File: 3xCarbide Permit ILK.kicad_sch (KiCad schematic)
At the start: 54 parts, among them J1 UT00104PH, J2 UT00104PH, J3 UT00104PH, J4 UT00104PH, J5 UT00104PH, J6 UT00104PH, SW1 2PB11, SW2 2PB11, SW3 2PB11, SW4 2PB11, SW5 2PB11, SW6 2PB11

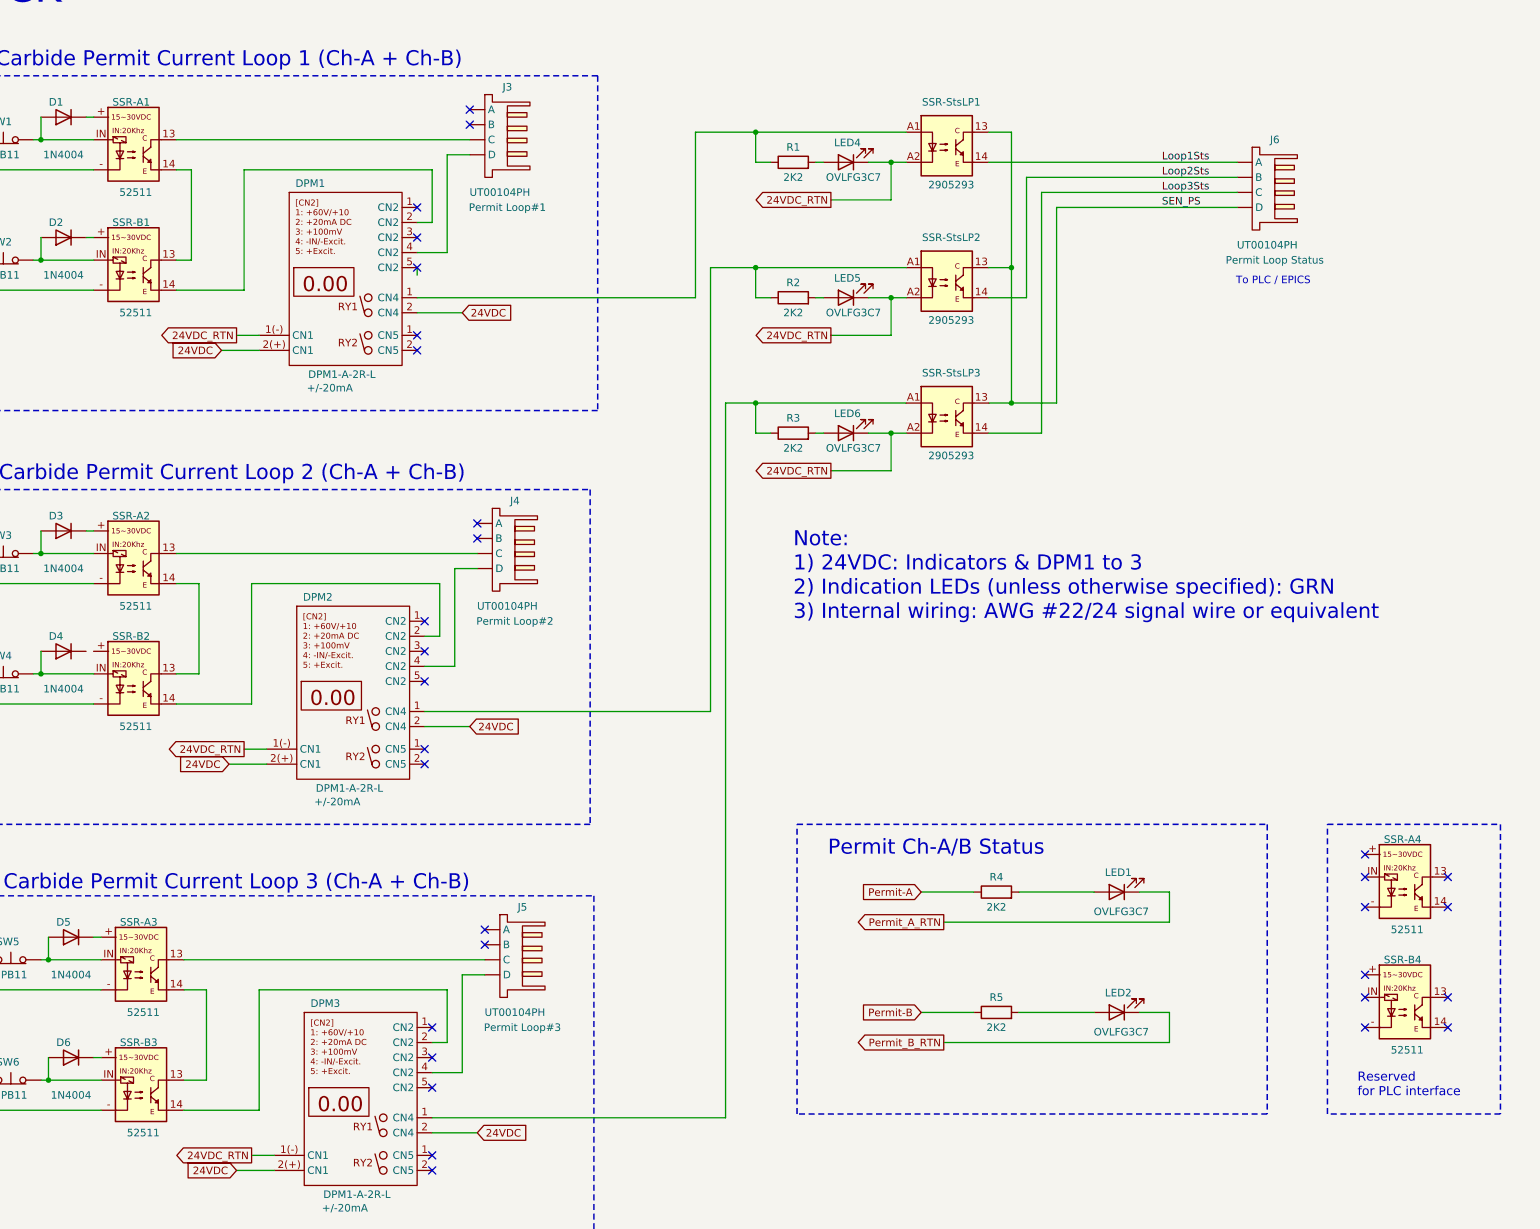
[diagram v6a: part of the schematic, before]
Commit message: updated 3input-SSR Lib
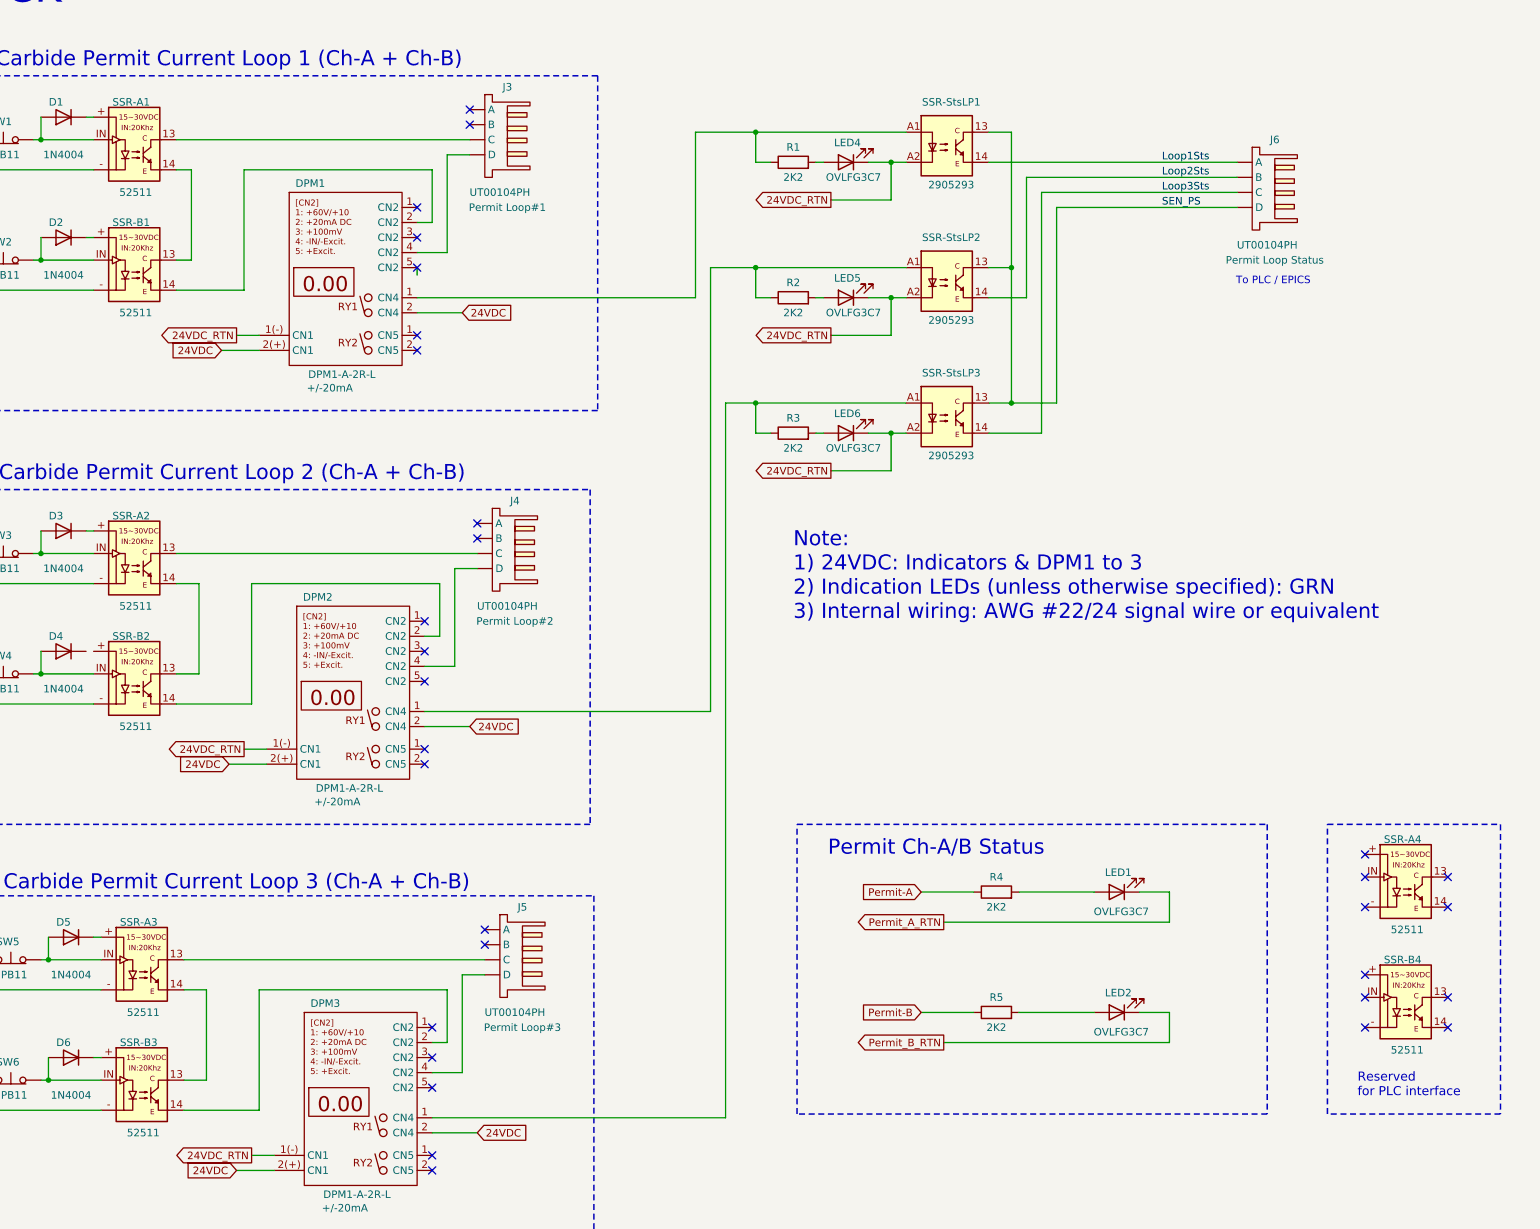
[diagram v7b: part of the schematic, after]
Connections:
- net at J2. (D): no longer TB-B1. (D)
- net at DPM1.1 (CN5): now also R1.1, SSR-StsLP1.A1
- net at J1. (D): now also TB-A3. (D)
- net at DPM3.1 (CN5): now also R3.1, SSR-StsLP3.A1
- net at J4. (D): now also DPM2.4 (CN2)
- net at J5. (D): now also SSR-A3.13
- new net: J2. (D), TB-B1. (D)
- new net: J1. (D), TB-A1. (D)
- new net: J2. (D), TB-B3. (D)
- now unconnected: J2. (D)
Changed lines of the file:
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@@
 		)
 		(instances
+			(project ".kicad_sch"
+				(path "/09dbfdd6-7cc7-4520-a5d9-a383f63872a0/2f06f779-eabb-4614-a40d-bb8dafaf0b3c"
+					(reference "R4")
+					(unit 1)
+				)
+			)
 			(project "3xCarbide Permit ILK"
 				(path "/2f06f779-eabb-4614-a40d-bb8dafaf0b3c"
@@
 		)
 		(instances
+			(project ".kicad_sch"
+				(path "/09dbfdd6-7cc7-4520-a5d9-a383f63872a0/2f06f779-eabb-4614-a40d-bb8dafaf0b3c"
+					(reference "D3")
+					(unit 1)
+				)
+			)
 			(project "3xCarbide Permit ILK"
 				(path "/2f06f779-eabb-4614-a40d-bb8dafaf0b3c"
@@
 		)
 		(instances
+			(project ".kicad_sch"
+				(path "/09dbfdd6-7cc7-4520-a5d9-a383f63872a0/2f06f779-eabb-4614-a40d-bb8dafaf0b3c"
+					(reference "D2")
+					(unit 1)
+				)
+			)
 			(project "3xCarbide Permit ILK"
 				(path "/2f06f779-eabb-4614-a40d-bb8dafaf0b3c"
@@
 		)
 		(instances
+			(project ".kicad_sch"
+				(path "/09dbfdd6-7cc7-4520-a5d9-a383f63872a0/2f06f779-eabb-4614-a40d-bb8dafaf0b3c"
+					(reference "SSR-StsLP1")
+					(unit 1)
+				)
+			)
 			(project "3xCarbide Permit ILK"
 				(path "/2f06f779-eabb-4614-a40d-bb8dafaf0b3c"
@@
 		)
 		(instances
+			(project ".kicad_sch"
+				(path "/09dbfdd6-7cc7-4520-a5d9-a383f63872a0/2f06f779-eabb-4614-a40d-bb8dafaf0b3c"
+					(reference "R2")
+					(unit 1)
+				)
+			)
 			(project "3xCarbide Permit ILK"
 				(path "/2f06f779-eabb-4614-a40d-bb8dafaf0b3c"
@@
 		)
 		(instances
+			(project ".kicad_sch"
+				(path "/09dbfdd6-7cc7-4520-a5d9-a383f63872a0/2f06f779-eabb-4614-a40d-bb8dafaf0b3c"
+					(reference "R5")
+					(unit 1)
+				)
+			)
 			(project "3xCarbide Permit ILK"
 				(path "/2f06f779-eabb-4614-a40d-bb8dafaf0b3c"
@@
 		)
 		(instances
+			(project ".kicad_sch"
+				(path "/09dbfdd6-7cc7-4520-a5d9-a383f63872a0/2f06f779-eabb-4614-a40d-bb8dafaf0b3c"
+					(reference "D1")
+					(unit 1)
+				)
+			)
 			(project "3xCarbide Permit ILK"
 				(path "/2f06f779-eabb-4614-a40d-bb8dafaf0b3c"
@@
 		)
 		(instances
+			(project ".kicad_sch"
+				(path "/09dbfdd6-7cc7-4520-a5d9-a383f63872a0/2f06f779-eabb-4614-a40d-bb8dafaf0b3c"
+					(reference "SSR-A4")
+					(unit 1)
+				)
+			)
 			(project "3xCarbide Permit ILK"
 				(path "/2f06f779-eabb-4614-a40d-bb8dafaf0b3c"
@@
 		)
 		(instances
+			(project ".kicad_sch"
+				(path "/09dbfdd6-7cc7-4520-a5d9-a383f63872a0/2f06f779-eabb-4614-a40d-bb8dafaf0b3c"
+					(reference "D6")
+					(unit 1)
+				)
+			)
 			(project "3xCarbide Permit ILK"
 				(path "/2f06f779-eabb-4614-a40d-bb8dafaf0b3c"
@@
 		)
 		(instances
+			(project ".kicad_sch"
+				(path "/09dbfdd6-7cc7-4520-a5d9-a383f63872a0/2f06f779-eabb-4614-a40d-bb8dafaf0b3c"
+					(reference "J3")
+					(unit 1)
+				)
+			)
 			(project "3xCarbide Permit ILK"
 				(path "/2f06f779-eabb-4614-a40d-bb8dafaf0b3c"
@@
 		)
 		(instances
+			(project ".kicad_sch"
+				(path "/09dbfdd6-7cc7-4520-a5d9-a383f63872a0/2f06f779-eabb-4614-a40d-bb8dafaf0b3c"
+					(reference "J4")
+					(unit 1)
+				)
+			)
 			(project "3xCarbide Permit ILK"
 				(path "/2f06f779-eabb-4614-a40d-bb8dafaf0b3c"
@@
 		)
 		(instances
+			(project ".kicad_sch"
+				(path "/09dbfdd6-7cc7-4520-a5d9-a383f63872a0/2f06f779-eabb-4614-a40d-bb8dafaf0b3c"
+					(reference "J5")
+					(unit 1)
+				)
+			)
 			(project "3xCarbide Permit ILK"
 				(path "/2f06f779-eabb-4614-a40d-bb8dafaf0b3c"
@@
 		)
 		(instances
+			(project ".kicad_sch"
+				(path "/09dbfdd6-7cc7-4520-a5d9-a383f63872a0/2f06f779-eabb-4614-a40d-bb8dafaf0b3c"
+					(reference "R3")
+					(unit 1)
+				)
+			)
 			(project "3xCarbide Permit ILK"
 				(path "/2f06f779-eabb-4614-a40d-bb8dafaf0b3c"
@@
 		)
 		(instances
+			(project ".kicad_sch"
+				(path "/09dbfdd6-7cc7-4520-a5d9-a383f63872a0/2f06f779-eabb-4614-a40d-bb8dafaf0b3c"
+					(reference "SSR-StsLP2")
+					(unit 1)
+				)
+			)
 			(project "3xCarbide Permit ILK"
 				(path "/2f06f779-eabb-4614-a40d-bb8dafaf0b3c"
@@
 		)
 		(instances
+			(project ".kicad_sch"
+				(path "/09dbfdd6-7cc7-4520-a5d9-a383f63872a0/2f06f779-eabb-4614-a40d-bb8dafaf0b3c"
+					(reference "D5")
+					(unit 1)
+				)
+			)
 			(project "3xCarbide Permit ILK"
 				(path "/2f06f779-eabb-4614-a40d-bb8dafaf0b3c"
@@
 		)
 		(instances
+			(project ".kicad_sch"
+				(path "/09dbfdd6-7cc7-4520-a5d9-a383f63872a0/2f06f779-eabb-4614-a40d-bb8dafaf0b3c"
+					(reference "D4")
+					(unit 1)
+				)
+			)
 			(project "3xCarbide Permit ILK"
 				(path "/2f06f779-eabb-4614-a40d-bb8dafaf0b3c"
@@
 		)
 		(instances
+			(project ".kicad_sch"
+				(path "/09dbfdd6-7cc7-4520-a5d9-a383f63872a0/2f06f779-eabb-4614-a40d-bb8dafaf0b3c"
+					(reference "J6")
+					(unit 1)
+				)
+			)
 			(project "3xCarbide Permit ILK"
 				(path "/2f06f779-eabb-4614-a40d-bb8dafaf0b3c"
@@
 		)
 		(instances
+			(project ".kicad_sch"
+				(path "/09dbfdd6-7cc7-4520-a5d9-a383f63872a0/2f06f779-eabb-4614-a40d-bb8dafaf0b3c"
+					(reference "SSR-StsLP3")
+					(unit 1)
+				)
+			)
 			(project "3xCarbide Permit ILK"
 				(path "/2f06f779-eabb-4614-a40d-bb8dafaf0b3c"
@@
 		)
 		(instances
+			(project ".kicad_sch"
+				(path "/09dbfdd6-7cc7-4520-a5d9-a383f63872a0/2f06f779-eabb-4614-a40d-bb8dafaf0b3c"
+					(reference "SSR-B4")
+					(unit 1)
+				)
+			)
 			(project "3xCarbide Permit ILK"
 				(path "/2f06f779-eabb-4614-a40d-bb8dafaf0b3c"
@@
 		)
 		(instances
+			(project ".kicad_sch"
+				(path "/09dbfdd6-7cc7-4520-a5d9-a383f63872a0/2f06f779-eabb-4614-a40d-bb8dafaf0b3c"
+					(reference "R1")
+					(unit 1)
+				)
+			)
 			(project "3xCarbide Permit ILK"
 				(path "/2f06f779-eabb-4614-a40d-bb8dafaf0b3c"
